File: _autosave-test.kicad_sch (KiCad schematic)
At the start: 35 parts, among them IC1 USBLC6-2SC6, IC2 ESP32-S3-WROOM-1-N16, J1 PWM, J2 UART0, SW1 Reset, SW2 Button, U1 USB-TYPE-C-018, U2 ADC08351CILQX{slash}NOPB, U3 ADC08351CILQX{slash}NOPB

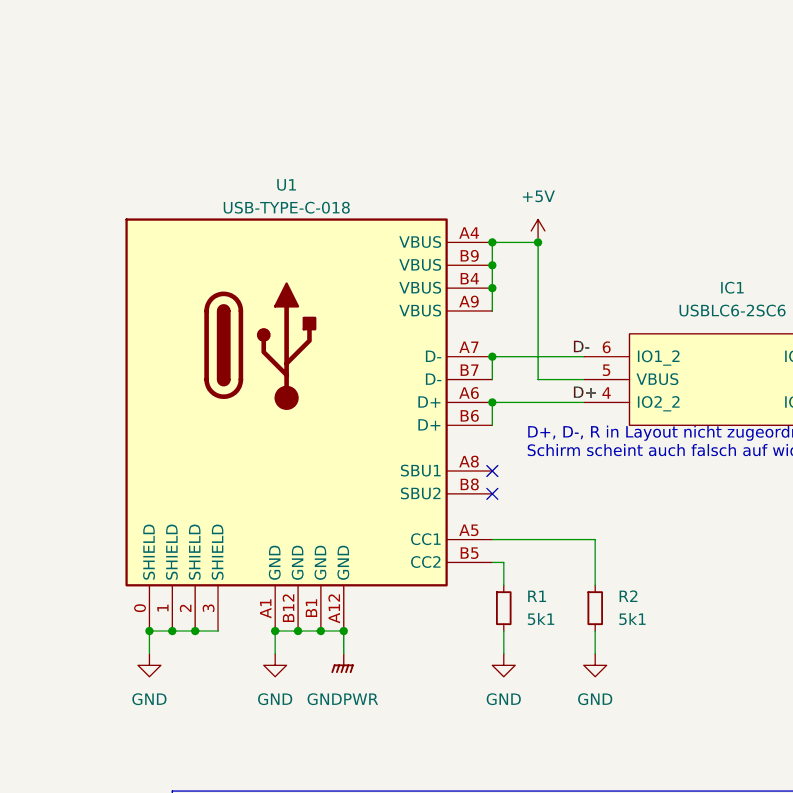
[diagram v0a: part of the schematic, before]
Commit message: Added ADC vor Trigger and changed Layout
Some Traces cant be good routed
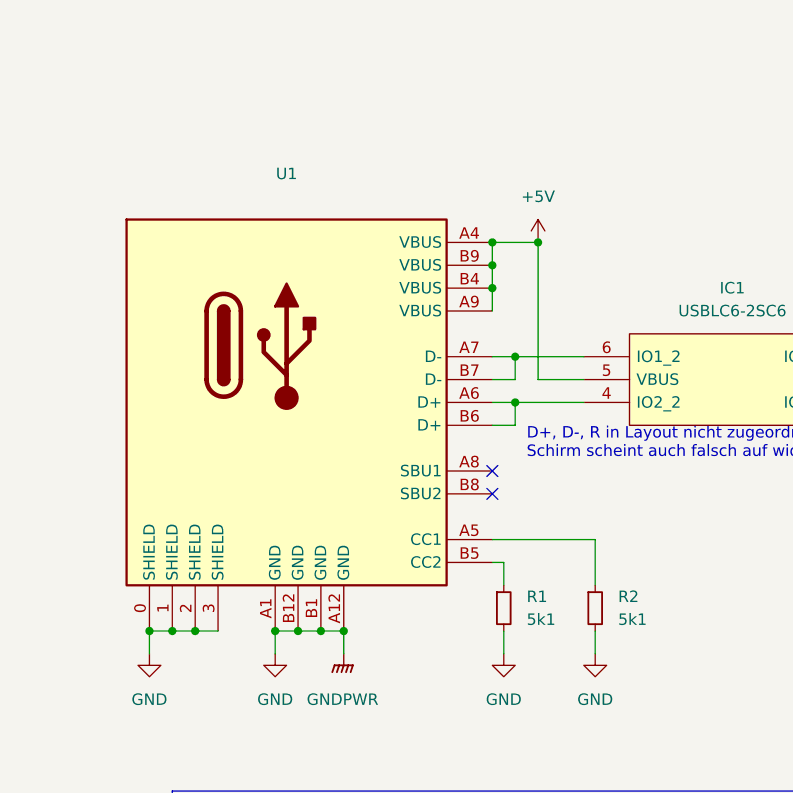
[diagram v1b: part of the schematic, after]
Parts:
- U1: value USB-TYPE-C-018 -> (none); footprint footprint:USB-C_SMD-TYPE-C-31-M-12 -> (none)
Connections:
- net D+: no longer names the net of IC1.4 (IO2_2), U1.A6 (D+), U1.B6 (D+)
- net D-: no longer names the net of IC1.6 (IO1_2), U1.A7 (D-), U1.B7 (D-)
